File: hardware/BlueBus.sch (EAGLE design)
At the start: 76 parts

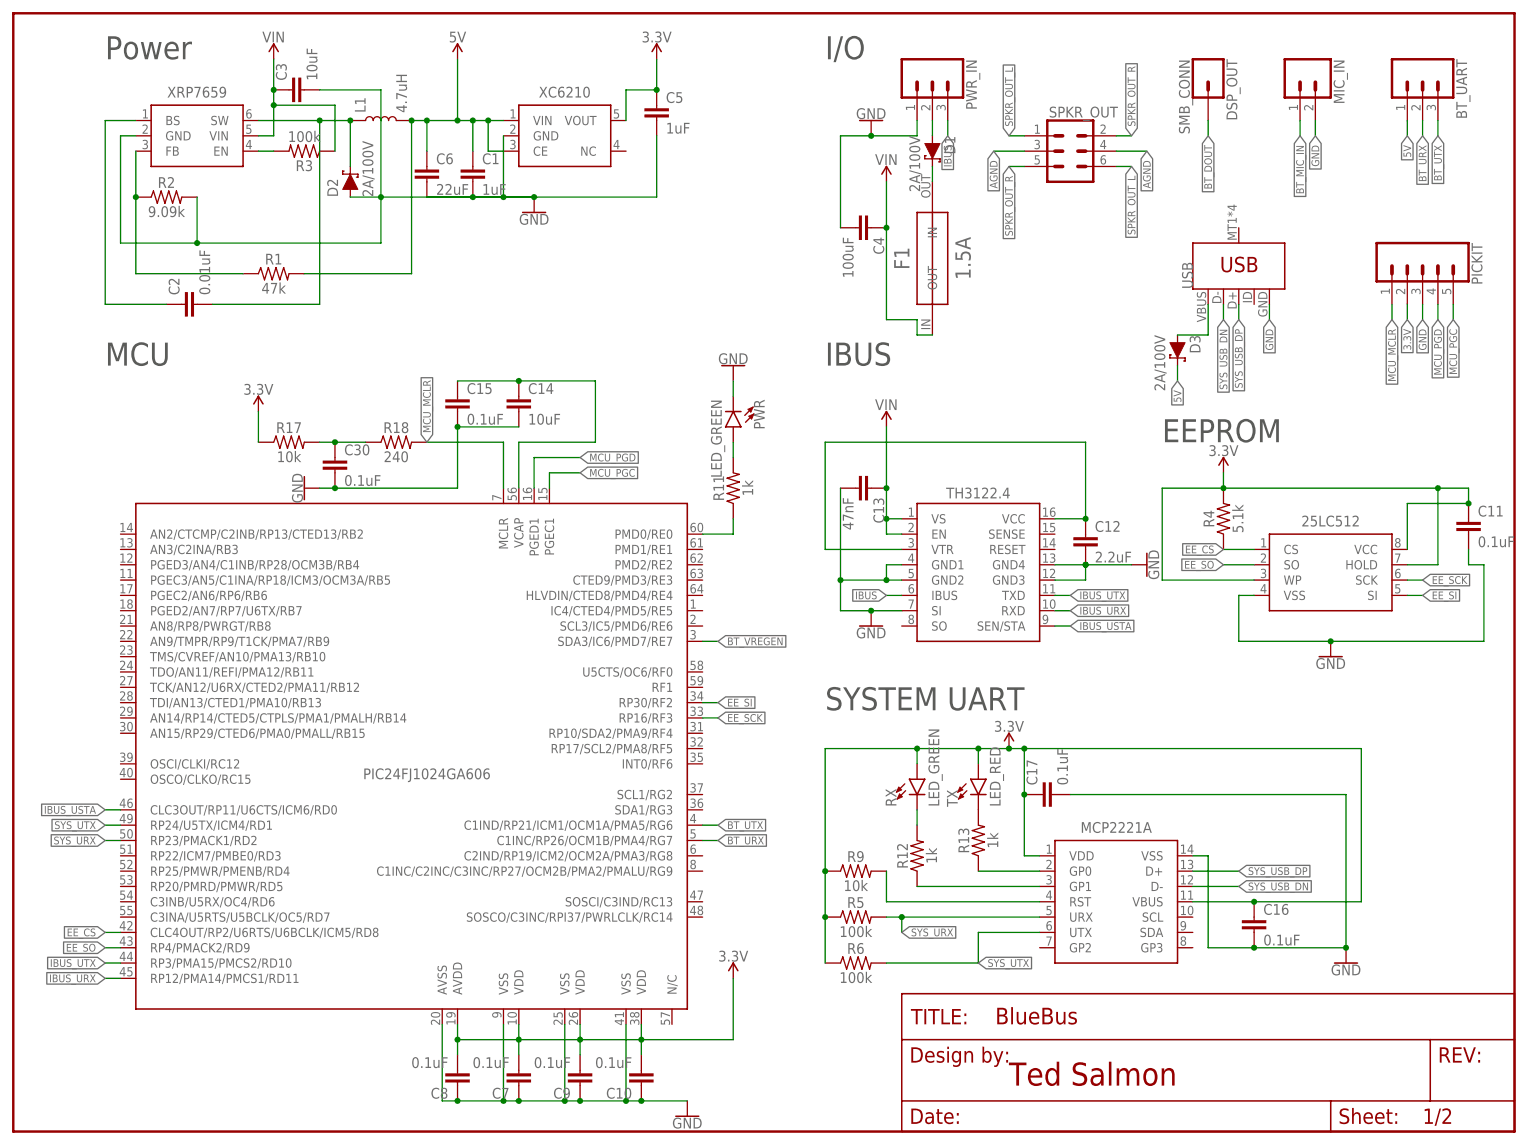
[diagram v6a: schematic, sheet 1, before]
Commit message: [IMP] hardware: BlueBus Rev A v4 * Add quad tri-state buffer to make system UART selectable between the MCU and BT module * Replace MCP2221A with FT232RQ in order to be able to use even parity UART for BT Module firmware updates
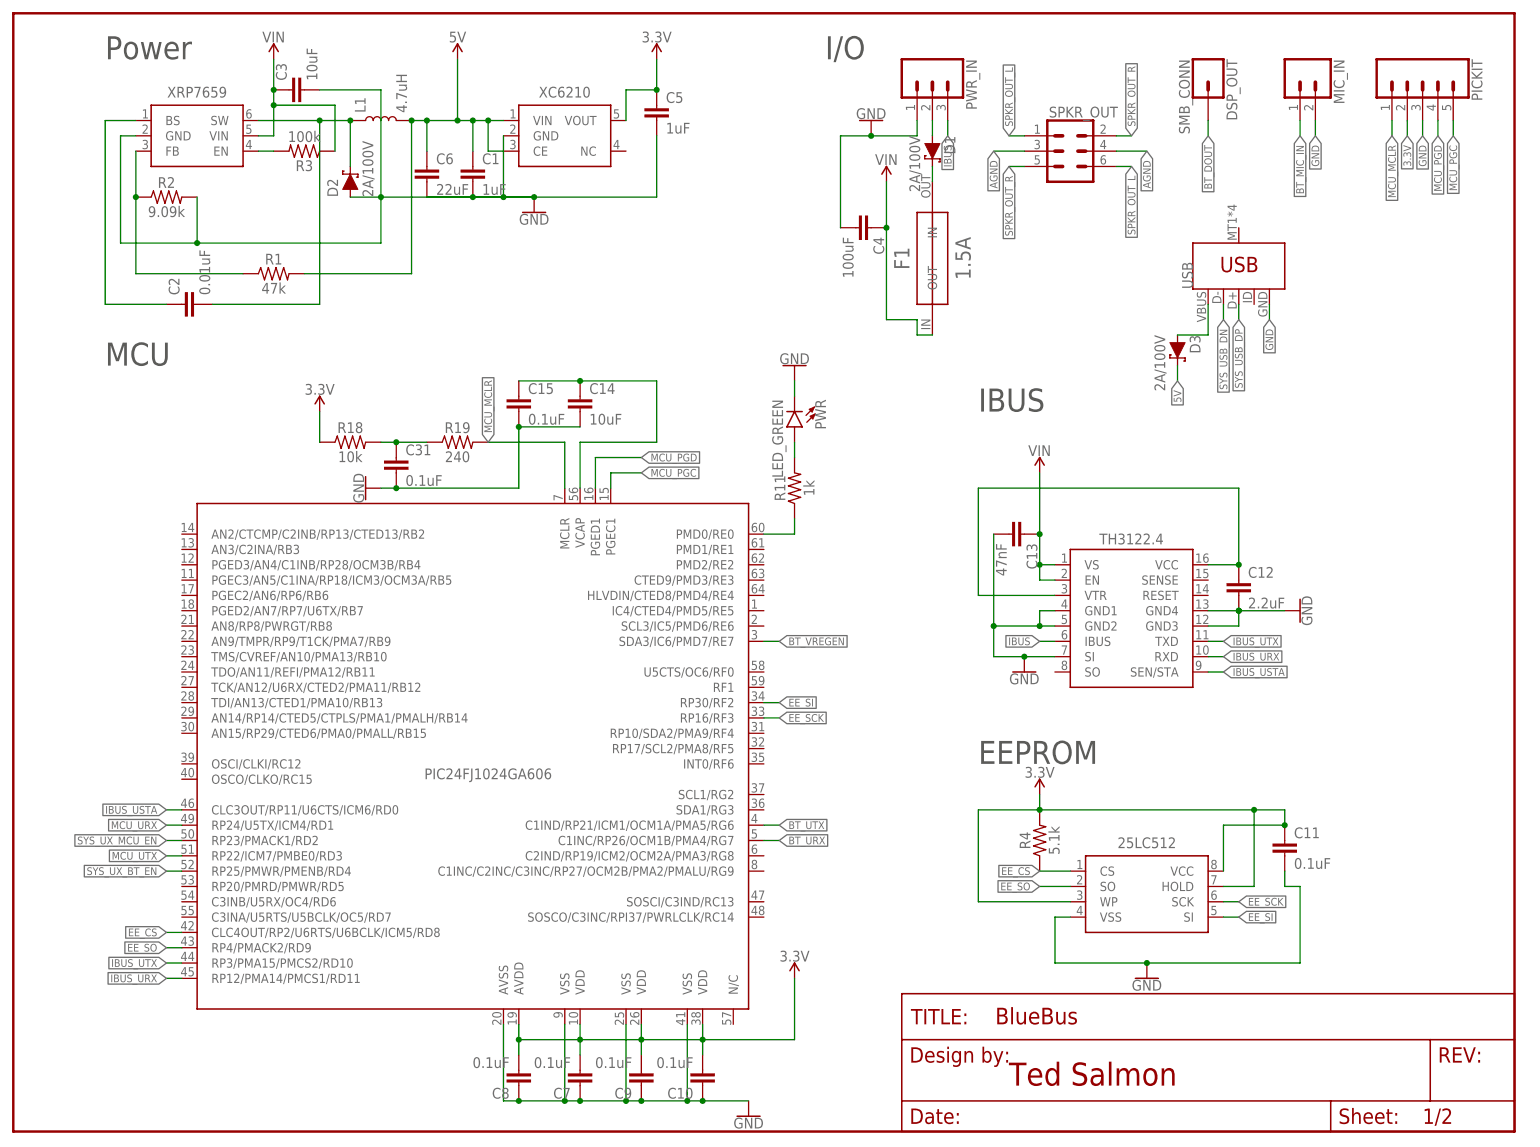
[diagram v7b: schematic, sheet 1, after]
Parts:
- removed BT_UART: (no value), SparkFun-Connectors:CONN_03
- removed MCP2221A: MCP2221A, ICs:MCP2221A
- removed R5: 100k, Passives:100KOHM
- added C32: 4.7uF, Passives:4.7UF
- added FT232RQ: FT232RQ, ICs:FT232RQ
- added R16: 470, Passives:470OHM
- added R21: 2k, Passives:2KOHM
- added SN74LVC125A: SN74LVC125A, ICs:SN74LVC125A
- C18: value 2.2nF -> 10uF; device Passives:2.2NF -> Passives:10UF2012
- C20: value 2.2uF -> 2.2nF; device Passives:2.2UF -> Passives:2.2NF
- C22: value 10uF -> 2.2uF; device Passives:10UF2012 -> Passives:2.2UF
- C23, C26, C28, C30: value 0.1uF -> 10uF; device Passives:0.1UF -> Passives:10UF2012
- C25, C27, C29: value 10uF -> 0.1uF; device Passives:10UF2012 -> Passives:0.1UF
- C31: value 4.7uF -> 0.1uF; device Passives:4.7UF -> Passives:0.1UF
- R10: value 10k -> 100k; device Passives:10KOHM -> Passives:100KOHM
- R14, R15: value 470 -> 100k; device Passives:470OHM -> Passives:100KOHM
- R17: value 10k -> 470; device Passives:10KOHM -> Passives:470OHM
- R18: value 240 -> 10k; device Passives:240OHM -> Passives:10KOHM
- R19: value 2 -> 240; device Passives:2OHM -> Passives:240OHM
- R20: value 2k -> 2; device Passives:2KOHM -> Passives:2OHM
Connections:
- removed net MCP_RST: MCP2221A.RST, R9.2
- removed net MCP_RX_LED: MCP2221A.GP1, R12.1
- removed net MCP_RX_LED_RES: R13.2, TX.C
- removed net MCP_TX_LED: MCP2221A.GP0, R13.1
- removed net MCP_TX_LED_RES: R12.2, RX.C
- new net MCU_URX: PIC24FJ1024GA606.RP24/U5TX/ICM4/RD1, R6.1, SN74LVC125A.3A
- new net MCU_UTX: PIC24FJ1024GA606.RP22/ICM7/PMBE0/RD3, R14.1, SN74LVC125A.4A
- new net SYS_RX_LED: FT232RQ.RXLED, RX.C
- new net SYS_RX_LED_RES: R12.1, RX.A
- new net SYS_TX_LED: FT232RQ.TXLED, TX.C
- new net SYS_TX_LED_RES: R13.1, TX.A
- new net SYS_UX_BT_EN: PIC24FJ1024GA606.RP25/PMWR/PMENB/RD4, R10.1, SN74LVC125A.1OE, SN74LVC125A.2OE
- new net SYS_UX_MCU_EN: PIC24FJ1024GA606.RP23/PMACK1/RD2, R15.1, SN74LVC125A.3OE, SN74LVC125A.4OE
- net 3.3V: now also C28.1, R12.2, R13.2, R14.2, R15.2, R18.1, R20.2, R6.2, R9.2, SN74LVC125A.VCC; no longer C17.1, C22.1, MCP2221A.VBUS, MCP2221A.VDD, R17.1, R19.2, R5.1, R6.1, R9.1, RX.A, TX.A
- net 5V: now also C17.1, C18.1, FT232RQ.VCC, FT232RQ.VCCIO; no longer BT_UART.1
- net AGND: now also C21.2, C26.2; no longer C18.2, C22.2
- net BT_3V3_FILTER: now also C32.1, R20.1; no longer C31.1, R19.1
- net BT_MIC_IN: now also R21.1; no longer R20.1
- net BT_RST: now also R9.1; no longer R10.1
- net BT_URX: now also SN74LVC125A.1A; no longer BT_UART.2
- net BT_UTX: now also SN74LVC125A.2A; no longer BT_UART.3
- net DAC_CAPM: now also C22.2; no longer C21.2
- net DAC_CAPP: now also C22.1; no longer C21.1
- net DAC_OUT_L: now also R16.2; no longer R14.2
- net DAC_OUT_R: now also R17.2; no longer R15.2
- net DAC_VNEG: now also C21.1; no longer C20.1
- net GND: now also C18.2, C32.2, FT232RQ.AGND, FT232RQ.GND17, FT232RQ.GND20, FT232RQ.GND4, FT232RQ.TEST, SN74LVC125A.GND; no longer C26.2, MCP2221A.VSS
- net LDOO: now also C30.1; no longer C28.1
- net MCU_MCLR: now also R19.2; no longer R18.2
- net MCU_MCLR_RES: now also C31.1, R18.2, R19.1; no longer C30.1, R17.2, R18.1
- net MIC_BIAS: now also R21.2; no longer R20.2
- net SPKR_OUT_L: now also C19.1, R16.1; no longer C18.1, R14.1
- net SPKR_OUT_R: now also C20.1, R17.1; no longer C19.1, R15.1
- net SYS_URX: now also FT232RQ.RXD, SN74LVC125A.2Y, SN74LVC125A.3Y; no longer MCP2221A.URX, PIC24FJ1024GA606.RP23/PMACK1/RD2, R5.2
- net SYS_USB_DN: now also FT232RQ.USBDM; no longer MCP2221A.D-
- net SYS_USB_DP: now also FT232RQ.USBDP; no longer MCP2221A.D+
- net SYS_UTX: now also FT232RQ.TXD, SN74LVC125A.1Y, SN74LVC125A.4Y; no longer MCP2221A.UTX, PIC24FJ1024GA606.RP24/U5TX/ICM4/RD1, R6.2
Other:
- note added: "System UART"
- note removed: "SYSTEM UART"
- moved on the sheet: C10, C11, C12, C13, C14, C15, C18, C19, C20, C21, C22, C23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

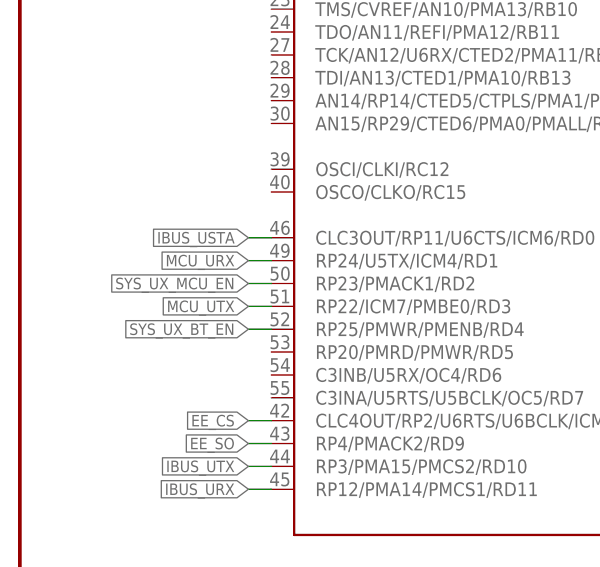
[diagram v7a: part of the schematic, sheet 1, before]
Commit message: [IMP] hardware: Minor Rewiring and alignment changes * Improve wiring around FT232R * Move passives around to allow more room for ground plane * Update Net Names so they make sense
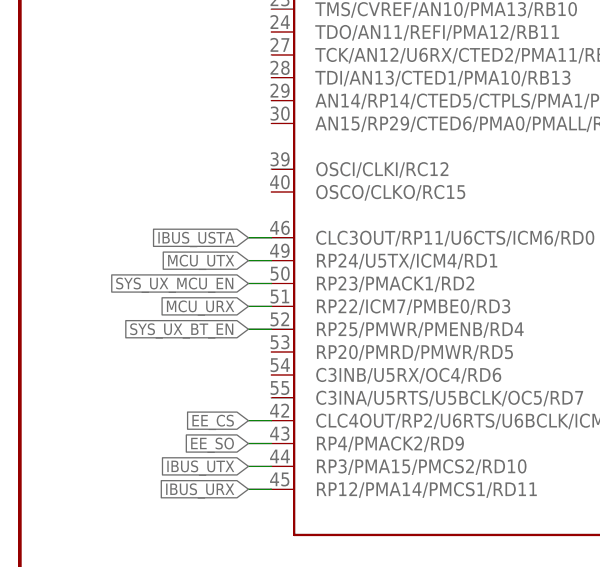
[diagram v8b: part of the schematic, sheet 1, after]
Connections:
- net MCU_URX: now also PIC24FJ1024GA606.RP22/ICM7/PMBE0/RD3, R14.1, SN74LVC125A.4A; no longer PIC24FJ1024GA606.RP24/U5TX/ICM4/RD1, R6.1, SN74LVC125A.3A
- net MCU_UTX: now also PIC24FJ1024GA606.RP24/U5TX/ICM4/RD1, R6.1, SN74LVC125A.3A; no longer PIC24FJ1024GA606.RP22/ICM7/PMBE0/RD3, R14.1, SN74LVC125A.4A
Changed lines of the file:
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@@
 <net name="MCU_UTX" class="5">
+<segment>
+<pinref part="PIC24FJ1024GA606" gate="G$1" pin="RP24/U5TX/ICM4/RD1"/>
+<wire x1="27.94" y1="50.8" x2="25.4" y2="50.8" width="0.1524" layer="91"/>
+<label x="25.4" y="50.8" size="1.27" layer="95" rot="R180" xref="yes"/>
+</segment>
+</net>
+<net name="SYS_UX_BT_EN" class="5">
+<segment>
+<pinref part="PIC24FJ1024GA606" gate="G$1" pin="RP25/PMWR/PMENB/RD4"/>
+<wire x1="27.94" y1="43.18" x2="25.4" y2="43.18" width="0.1524" layer="91"/>
+<label x="25.4" y="43.18" size="1.27" layer="95" rot="R180" xref="yes"/>
+</segment>
+</net>
+<net name="SYS_UX_MCU_EN" class="5">
+<segment>
+<pinref part="PIC24FJ1024GA606" gate="G$1" pin="RP23/PMACK1/RD2"/>
+<wire x1="27.94" y1="48.26" x2="25.4" y2="48.26" width="0.1524" layer="91"/>
+<label x="25.4" y="48.26" size="1.27" layer="95" rot="R180" xref="yes"/>
+</segment>
+</net>
+<net name="MCU_URX" class="5">
 <segment>
 <pinref part="PIC24FJ1024GA606" gate="G$1" pin="RP22/ICM7/PMBE0/RD3"/>
 <wire x1="27.94" y1="45.72" x2="25.4" y2="45.72" width="0.1524" layer="91"/>
 <label x="25.4" y="45.72" size="1.27" layer="95" rot="R180" xref="yes"/>
-</segment>
-</net>
-<net name="MCU_URX" class="5">
-<segment>
-<pinref part="PIC24FJ1024GA606" gate="G$1" pin="RP24/U5TX/ICM4/RD1"/>
-<wire x1="27.94" y1="50.8" x2="25.4" y2="50.8" width="0.1524" layer="91"/>
-<label x="25.4" y="50.8" size="1.27" layer="95" rot="R180" xref="yes"/>
-</segment>
-</net>
-<net name="SYS_UX_BT_EN" class="5">
-<segment>
-<pinref part="PIC24FJ1024GA606" gate="G$1" pin="RP25/PMWR/PMENB/RD4"/>
-<wire x1="27.94" y1="43.18" x2="25.4" y2="43.18" width="0.1524" layer="91"/>
-<label x="25.4" y="43.18" size="1.27" layer="95" rot="R180" xref="yes"/>
-</segment>
-</net>
-<net name="SYS_UX_MCU_EN" class="5">
-<segment>
-<pinref part="PIC24FJ1024GA606" gate="G$1" pin="RP23/PMACK1/RD2"/>
-<wire x1="27.94" y1="48.26" x2="25.4" y2="48.26" width="0.1524" layer="91"/>
-<label x="25.4" y="48.26" size="1.27" layer="95" rot="R180" xref="yes"/>
 </segment>
 </net>
@@
 </segment>
 </net>
-<net name="MCU_UTX" class="5">
+<net name="MCU_URX" class="5">
 <segment>
 <pinref part="SN74LVC125A" gate="G$1" pin="4A"/>
@@
 </segment>
 </net>
-<net name="MCU_URX" class="5">
+<net name="MCU_UTX" class="5">
 <segment>
 <pinref part="SN74LVC125A" gate="G$1" pin="3A"/>
